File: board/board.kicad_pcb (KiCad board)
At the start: 2 copper layers, 61 x 13 mm, 36 parts, among them J1 USB4105-GF-A, J2 100_digital_IO, J3 SWD_6_Pol_Needle, J4 100_digital_IO, SW1 PTS636 SK25J SMTR LFS, U1 W25Q16JVUXIQ, U2 RP2040, U3 TLV743P, Y1 12MhZ

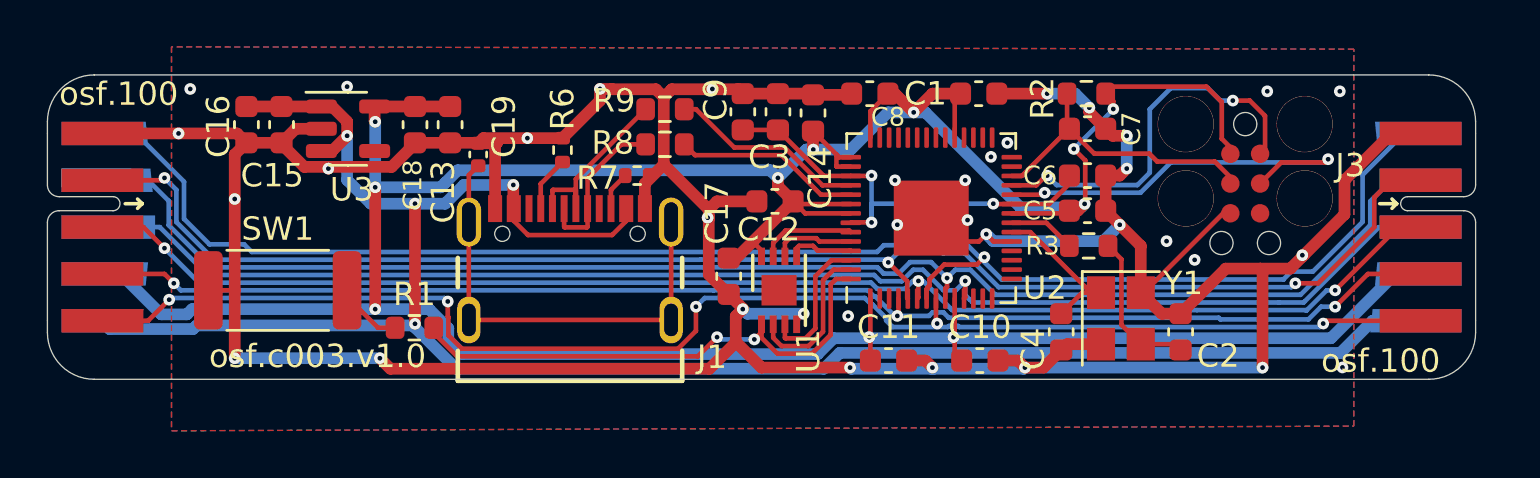
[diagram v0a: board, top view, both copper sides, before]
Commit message: added straping support for different interfaces
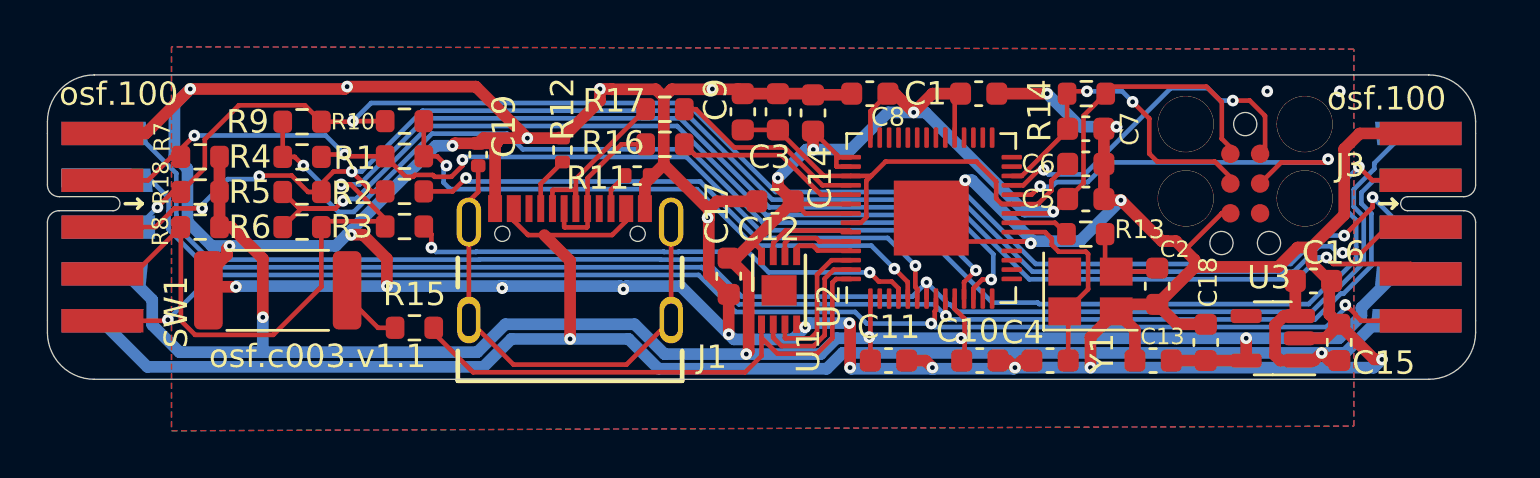
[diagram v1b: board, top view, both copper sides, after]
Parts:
- added R1: 0R, Resistor_SMD:R_0603_1608Metric, F.Cu at (155.2, 93.5)
- added R10: 0R, Resistor_SMD:R_0603_1608Metric, F.Cu at (155.2, 92.0)
- added R18: 10k, Resistor_SMD:R_0603_1608Metric, F.Cu at (146.5, 95.0)
- added R2: 0R, Resistor_SMD:R_0603_1608Metric, F.Cu at (155.2, 95.0)
- added R3: 0R, Resistor_SMD:R_0603_1608Metric, F.Cu at (155.2, 96.5)
- added R4: 0R, Resistor_SMD:R_0603_1608Metric, F.Cu at (150.9, 93.5)
- added R5: 0R, Resistor_SMD:R_0603_1608Metric, F.Cu at (150.9, 95.0)
- added R6: 0R, Resistor_SMD:R_0603_1608Metric, F.Cu at (150.9, 96.5)
- added R7: 2k, Resistor_SMD:R_0603_1608Metric, F.Cu at (146.5, 93.5)
- added R8: 2k, Resistor_SMD:R_0603_1608Metric, F.Cu at (146.5, 96.5)
- added R9: 0R, Resistor_SMD:R_0603_1608Metric, F.Cu at (150.9, 92.0)
- moved C15 46.1 mm to (195.2, 101.4), turned to 90 degrees
- moved C16 46.1 mm to (194.1, 98.8), turned to 0 degrees
- moved U3 40.5 mm to (192.3, 101.2), turned to 180 degrees
- moved C18 35.0 mm to (189.5, 101.4), turned to 90 degrees
- moved C13 31.7 mm to (187.2, 102.2), turned to 180 degrees
- moved C2 2.19 mm to (187.4, 99.0), turned to -90 degrees
- moved Y1 1.74 mm to (184.6, 99.2), turned to 0 degrees
- moved C4 1.31 mm to (182.8, 102.2), turned to 180 degrees
- moved R13 0.52 mm to (184.3, 96.8)
- moved C5 0.51 mm to (184.3, 95.3)
- moved C6 0.51 mm to (184.3, 93.8)
- moved C7 0.08 mm to (184.3, 92.3)
- renumbered R7 to R11, R6 to R12, R3 to R13, R2 to R14, R1 to R15, R8 to R16, R9 to R17
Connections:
- net /rp2040/GPIO6 renamed /GPIO6
- net /rp2040/GPIO7 renamed /GPIO7
- net /rp2040/~{SPI0_CS} renamed /GPIO5
- J2 pad 2: /rp2040/SPI0_TX -> Net-(J2-IO0)
- J2 pad 3: /rp2040/SPI0_RX -> Net-(J2-IO1)
- J2 pad 4: /rp2040/SPI0_SCK -> Net-(J2-IO2)
- J2 pad 8: /rp2040/UART1_TX -> Net-(J2-IO6)
- J4 pad 2: /rp2040/SPI0_TX -> Net-(J2-IO0)
- J4 pad 3: /rp2040/SPI0_RX -> Net-(J2-IO1)
- J4 pad 4: /rp2040/SPI0_SCK -> Net-(J2-IO2)
- J4 pad 8: /rp2040/UART1_TX -> Net-(J2-IO6)
- U2 pad 11: /rp2040/UART1_TX -> /GPIO0
- U2 pad 12: /rp2040/UART1_RX -> /GPIO1
- U2 pad 4: /rp2040/SPI0_SCK -> /GPIO2
- U2 pad 5: /rp2040/SPI0_TX -> /GPIO3
- U2 pad 6: /rp2040/SPI0_RX -> /GPIO4
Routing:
- net Net-(J2-IO2): track 0.00 -> 74.4 mm, vias 0 -> 2
- net Net-(J2-IO0): track 0.00 -> 67.5 mm, vias 0 -> 4
- net Net-(J2-IO6): track 0.00 -> 65.7 mm, vias 0 -> 4
- net Net-(J2-IO1): track 0.00 -> 65.0 mm, vias 0 -> 4
- net /rp2040/SPI0_TX: track 63.9 -> 0.00 mm, vias 3 -> 0
- net /rp2040/UART1_TX: track 60.6 -> 0.00 mm, vias 1 -> 0
- net /rp2040/SPI0_RX: track 60.3 -> 0.00 mm, vias 3 -> 0
- net /rp2040/SPI0_SCK: track 58.8 -> 0.00 mm, vias 3 -> 0
- net /GPIO1: track 0.00 -> 39.4 mm, vias 0 -> 2
- net /GPIO0: track 0.00 -> 37.6 mm, vias 0 -> 2
- net GND: track 173.3 -> 207.5 mm, vias 36 -> 28
- net /GPIO3: track 0.00 -> 25.7 mm, vias 0 -> 2
- net /GPIO4: track 0.00 -> 24.2 mm, vias 0 -> 2
- net /GPIO2: track 0.00 -> 22.2 mm, vias 0 -> 2
- net +3V3: track 149.9 -> 137.3 mm, vias 11 -> 9
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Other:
- board text added: "osf.c003.v1.1"
- board text removed: "osf.c003.v1.0"
